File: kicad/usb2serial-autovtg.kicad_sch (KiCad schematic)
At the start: 38 parts, among them J2 Conn_01x04, J3 USB_C_Receptacle_USB2.0, U1 FT234XD, U3 74LVC1G17GW, U5 LMV358AIDGKR, U6 74LVC1G17GW

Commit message: 1.2V: wip
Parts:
- removed D4: BZX84C2V4LT1, Package_TO_SOT_SMD:SOT-23, symbol Diode:BZX84Cxx
- removed R15: 120, Resistor_SMD:R_0402_1005Metric, symbol Device:R
- removed U3, U6: 74LVC1G17GW, Package_SO:TSOP-5_1.65x3.05mm_P0.95mm, symbol ft234xd:74LVC1G17
- added U2, U4: 74LVC1T45GW, Package_TO_SOT_SMD:SOT-363_SC-70-6, symbol Logic_LevelTranslator:SN74LVC1T45DCK
- added U7: TLV74112PDBVR, Package_TO_SOT_SMD:SOT-23-5, symbol Regulator_Linear:TLV70012_SOT23-5
- C5: value 0.1u -> 1u
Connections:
- net +3V3: now also U2.1 (VCCA), U2.5 (DIR), U4.1 (VCCA), U7.1 (IN), U7.3 (EN)
- net GND: now also U2.2 (GND), U4.2 (GND), U4.5 (DIR), U7.2 (GND)
- net at U1.10 (RXD): now also U4.3 (A)
- net at U1.7 (TXD): now also U2.3 (A)
- net at R12.2, R3.1, R5.2: now also U4.4 (B)
- net at C10.1, R10.2: now also U2.6 (VCCB)
- net at R11.2: now also U2.4 (B)
- net +2V5 renamed +1V2
- net +1V2: now also U4.6 (VCCB), U7.5 (OUT)
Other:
- note added: "Vtarget range: 1.2V .. ~5.0V"
- note removed: "RX 74LVC1G17: @Vdd=2.5V: positive-going threshold: <=1.5V FT234 VddIO: 3.3V - positive-going threshold: <= 2.0V"
- note removed: "TX 74LVC1G17: @Vdd=5V: positive-going threshold: <=2.6V FT234 VddIO: 3.3V"
- note removed: "Vtarget range: 1.8V .. ~5.0V"
- moved on the sheet: C5, D1, R11, R12, R4, R5

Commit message: wip
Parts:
- added C7: 0.1u/10V, Capacitor_SMD:C_0402_1005Metric, symbol Device:C
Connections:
- net +3V3: now also C7.1
- net GND: now also C7.2
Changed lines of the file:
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@@
   (junction (at 189.23 137.16) (diameter 0) (color 0 0 0 0)
   )
+  (junction (at 163.83 123.19) (diameter 0) (color 0 0 0 0)
+  )
   (junction (at 86.36 153.67) (diameter 0) (color 0 0 0 0)
   )
@@
     (stroke (width 0) (type default))
   )
-  (wire (pts (xy 156.21 110.49) (xy 156.21 134.62))
+  (wire (pts (xy 139.7 110.49) (xy 139.7 134.62))
     (stroke (width 0) (type default))
   )
@@
     (stroke (width 0) (type default))
   )
+  (wire (pts (xy 163.83 123.19) (xy 163.83 127))
+    (stroke (width 0) (type default))
+  )
   (wire (pts (xy 102.87 33.02) (xy 118.11 33.02))
     (stroke (width 0) (type default))
@@
     (stroke (width 0) (type default))
   )
-  (wire (pts (xy 167.64 110.49) (xy 156.21 110.49))
+  (wire (pts (xy 167.64 110.49) (xy 139.7 110.49))
     (stroke (width 0) (type default))
   )
@@
     (stroke (width 0) (type default))
   )
-  (wire (pts (xy 156.21 134.62) (xy 135.89 134.62))
+  (wire (pts (xy 139.7 134.62) (xy 135.89 134.62))
     (stroke (width 0) (type default))
   )
@@
     )
   )
+  (symbol (lib_id "power:GND") (at 156.21 123.19 0) (unit 1)
+    (in_bom yes) (on_board yes) (dnp no)
+    (property "Reference" "#PWR036" (at 156.21 129.54 0)
+      (effects (font (size 1.27 1.27)) hide)
+    )
+    (property "Value" "GND" (at 156.337 127.5842 0)
+      (effects (font (size 1.27 1.27)))
+    )
+    (property "Footprint" "" (at 156.21 123.19 0)
+      (effects (font (size 1.27 1.27)) hide)
+    )
+    (property "Datasheet" "" (at 156.21 123.19 0)
+      (effects (font (size 1.27 1.27)) hide)
+    )
+    (pin "1")
+    (instances
+      (project "usb2serial-autovtg"
+        (path "/1f08e041-63eb-4c92-ae2b-bdba754c2965"
+          (reference "#PWR036") (unit 1)
+        )
+      )
+    )
+  )
   (symbol (lib_id "power:GND") (at 68.58 167.64 0) (unit 1)
     (in_bom yes) (on_board yes) (dnp no)
@@
     )
   )
-  (symbol (lib_id "power:+3V3") (at 163.83 127 0) (unit 1)
-    (in_bom yes) (on_board yes) (dnp no)
-    (property "Reference" "#PWR016" (at 163.83 130.81 0)
-      (effects (font (size 1.27 1.27)) hide)
-    )
-    (property "Value" "+3V3" (at 162.56 123.19 0)
-      (effects (font (size 1.27 1.27)))
-    )
-    (property "Footprint" "" (at 163.83 127 0)
-      (effects (font (size 1.27 1.27)) hide)
-    )
-    (property "Datasheet" "" (at 163.83 127 0)
+  (symbol (lib_id "power:+3V3") (at 163.83 123.19 0) (unit 1)
+    (in_bom yes) (on_board yes) (dnp no)
+    (property "Reference" "#PWR016" (at 163.83 127 0)
+      (effects (font (size 1.27 1.27)) hide)
+    )
+    (property "Value" "+3V3" (at 162.56 119.38 0)
+      (effects (font (size 1.27 1.27)))
+    )
+    (property "Footprint" "" (at 163.83 123.19 0)
+      (effects (font (size 1.27 1.27)) hide)
+    )
+    (property "Datasheet" "" (at 163.83 123.19 0)
       (effects (font (size 1.27 1.27)) hide)
     )
@@
         )
       )
+    )
+  )
+  (symbol (lib_id "Device:C") (at 160.02 123.19 270) (unit 1)
+    (in_bom yes) (on_board yes) (dnp no)
+    (property "Reference" "C7" (at 160.02 125.73 0)
+      (effects (font (size 1.27 1.27)) (justify left) hide)
+    )
+    (property "Value" "0.1u/10V" (at 149.86 119.38 90)
+      (effects (font (size 1.27 1.27)) (justify left))
+    )
+    (property "Footprint" "Capacitor_SMD:C_0402_1005Metric" (at 156.21 124.1552 0)
+      (effects (font (size 1.27 1.27)) hide)
+    )
+    (property "Datasheet" "" (at 160.02 123.19 0)
+      (effects (font (size 1.27 1.27)) hide)
+    )
+    (pin "1")
+    (pin "2")
+    (instances
+      (project "usb2serial-autovtg"
+        (path "/1f08e041-63eb-4c92-ae2b-bdba754c2965"
+          (reference "C7") (unit 1)
+        )
+      )

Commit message: add note regarding DIR pin
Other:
- note added: "DIR HIGH: A to B DIR LOW: B to A"
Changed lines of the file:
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@@
     (stroke (width 0) (type default))
+  )
+  (text "DIR HIGH: A to B\nDIR LOW: B to A" (at 189.23 100.33 0)
+    (effects (font (size 1.27 1.27) (thickness 0.254) bold) (justify left bottom))
   )
   (text "CBUS0 must be configured for ~{TX&RXLED} during production:\n  Option 1: http://www.ftdichip.com/Support/Utilities.htm#FT_Prog (Windows)\n  Option 2: https://github.com/richardeoin/ftx-prog (Linux)"

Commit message: finalize rev3
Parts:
- C5: value 1u -> 4.7u/10V
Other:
- note removed: "BZX84C2V4LT1: I_{ZT}: ~6.5mA => V_{Z}: ~2.5V"
- moved on the sheet: C5, U7
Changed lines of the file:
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@@
   (title_block
     (title "USB2serial AutoVtg")
-    (date "2023-07-28")
-    (rev "v2")
+    (date "2024-01-23")
+    (rev "v3")
     (comment 1 "     https://creativecommons.org/licenses/by-sa/4.0/deed.en")
     (comment 2 "License: Creative Commons Attribution/Share-Alike 4.0")
     (comment 3 "Designed by: Benedikt Heinz <hunz at mailbox.org>")
   )
-  (junction (at 26.67 26.67) (diameter 0) (color 0 0 0 0)
+  (junction (at 43.18 34.29) (diameter 0) (color 0 0 0 0)
   )
   (junction (at 231.14 130.81) (diameter 0) (color 0 0 0 0)
@@
   (junction (at 88.9 85.09) (diameter 0) (color 0 0 0 0)
   )
-  (junction (at 44.45 26.67) (diameter 0) (color 0 0 0 0)
+  (junction (at 60.96 34.29) (diameter 0) (color 0 0 0 0)
   )
   (junction (at 166.37 147.32) (diameter 0) (color 0 0 0 0)
@@
     (stroke (width 0) (type default))
   )
-  (wire (pts (xy 26.67 24.13) (xy 26.67 26.67))
-    (stroke (width 0) (type default))
-  )
-  (wire (pts (xy 26.67 26.67) (xy 26.67 29.21))
+  (wire (pts (xy 43.18 31.75) (xy 43.18 34.29))
+    (stroke (width 0) (type default))
+  )
+  (wire (pts (xy 43.18 34.29) (xy 43.18 36.83))
     (stroke (width 0) (type default))
   )
@@
     (stroke (width 0) (type default))
   )
-  (wire (pts (xy 41.91 26.67) (xy 44.45 26.67))
+  (wire (pts (xy 58.42 34.29) (xy 60.96 34.29))
     (stroke (width 0) (type default))
   )
@@
     (at 100.33 167.64 0)
     (effects (font (size 1.27 1.27)) (justify left bottom) (href "https://github.com/richardeoin/ftx-prog"))
-  )
-  (text "BZX84C2V4LT1:\n  I_{ZT}: ~6.5mA => V_{Z}: ~2.5V" (at 53.34 58.42 0)
-    (effects (font (size 1.27 1.27)) (justify left bottom))
   )
   (text "SBOS923H (TI LMV3xxA / 6.1 Absolute Maximum Ratings) states:\n Input pins are diode-clamped to the power-supply rails.\n Input signals that may swing more than 0.5 V beyond the\n supply rails must be current limited to 10 mA or less.\n\nR6 limits the clamping current when VTG is supplied\n with no USB supply connected."
@@
     )
   )
-  (symbol (lib_id "power:GND") (at 34.29 36.83 0) (unit 1)
-    (in_bom yes) (on_board yes) (dnp no)
-    (property "Reference" "#PWR034" (at 34.29 43.18 0)
-      (effects (font (size 1.27 1.27)) hide)
-    )
-    (property "Value" "GND" (at 34.417 41.2242 0)
-      (effects (font (size 1.27 1.27)))
-    )
-    (property "Footprint" "" (at 34.29 36.83 0)
-      (effects (font (size 1.27 1.27)) hide)
-    )
-    (property "Datasheet" "" (at 34.29 36.83 0)
+  (symbol (lib_id "power:GND") (at 50.8 44.45 0) (unit 1)
+    (in_bom yes) (on_board yes) (dnp no)
+    (property "Reference" "#PWR034" (at 50.8 50.8 0)
+      (effects (font (size 1.27 1.27)) hide)
+    )
+    (property "Value" "GND" (at 50.927 48.8442 0)
+      (effects (font (size 1.27 1.27)))
+    )
+    (property "Footprint" "" (at 50.8 44.45 0)
+      (effects (font (size 1.27 1.27)) hide)
+    )
+    (property "Datasheet" "" (at 50.8 44.45 0)
       (effects (font (size 1.27 1.27)) hide)
     )
@@
     )
   )
-  (symbol (lib_id "power:GND") (at 44.45 34.29 0) (unit 1)
-    (in_bom yes) (on_board yes) (dnp no)
-    (property "Reference" "#PWR015" (at 44.45 40.64 0)
-      (effects (font (size 1.27 1.27)) hide)
-    )
-    (property "Value" "GND" (at 44.577 38.6842 0)
-      (effects (font (size 1.27 1.27)))
-    )
-    (property "Footprint" "" (at 44.45 34.29 0)
-      (effects (font (size 1.27 1.27)) hide)
-    )
-    (property "Datasheet" "" (at 44.45 34.29 0)
+  (symbol (lib_id "power:GND") (at 60.96 41.91 0) (unit 1)
+    (in_bom yes) (on_board yes) (dnp no)
+    (property "Reference" "#PWR015" (at 60.96 48.26 0)
+      (effects (font (size 1.27 1.27)) hide)
+    )
+    (property "Value" "GND" (at 61.087 46.3042 0)
+      (effects (font (size 1.27 1.27)))
+    )
+    (property "Footprint" "" (at 60.96 41.91 0)
+      (effects (font (size 1.27 1.27)) hide)
+    )
+    (property "Datasheet" "" (at 60.96 41.91 0)
       (effects (font (size 1.27 1.27)) hide)
     )
@@
     )
   )
-  (symbol (lib_id "Device:C") (at 44.45 30.48 0) (unit 1)
-    (in_bom yes) (on_board yes) (dnp no)
-    (property "Reference" "C5" (at 47.3456 29.3116 0)
-      (effects (font (size 1.27 1.27)) (justify left))
-    )
-    (property "Value" "1u" (at 47.3456 31.623 0)
-      (effects (font (size 1.27 1.27)) (justify left))
-    )
-    (property "Footprint" "Capacitor_SMD:C_0402_1005Metric" (at 45.4152 34.29 0)
-      (effects (font (size 1.27 1.27)) hide)
-    )
-    (property "Datasheet" "" (at 44.45 30.48 0)
+  (symbol (lib_id "Device:C") (at 60.96 38.1 0) (unit 1)
+    (in_bom yes) (on_board yes) (dnp no)
+    (property "Reference" "C5" (at 63.8556 36.9316 0)
+      (effects (font (size 1.27 1.27)) (justify left))
+    )
+    (property "Value" "4.7u/10V" (at 63.8556 39.243 0)
+      (effects (font (size 1.27 1.27)) (justify left))
+    )
+    (property "Footprint" "Capacitor_SMD:C_0402_1005Metric" (at 61.9252 41.91 0)
+      (effects (font (size 1.27 1.27)) hide)
+    )
+    (property "Datasheet" "" (at 60.96 38.1 0)
       (effects (font (size 1.27 1.27)) hide)
     )
@@
     )
   )
-  (symbol (lib_id "power:+3V3") (at 26.67 24.13 0) (unit 1)
-    (in_bom yes) (on_board yes) (dnp no)
-    (property "Reference" "#PWR017" (at 26.67 27.94 0)
-      (effects (font (size 1.27 1.27)) hide)
-    )
-    (property "Value" "+3V3" (at 26.67 20.32 0)
-      (effects (font (size 1.27 1.27)))
-    )
-    (property "Footprint" "" (at 26.67 24.13 0)
-      (effects (font (size 1.27 1.27)) hide)
-    )
-    (property "Datasheet" "" (at 26.67 24.13 0)
+  (symbol (lib_id "power:+3V3") (at 43.18 31.75 0) (unit 1)
+    (in_bom yes) (on_board yes) (dnp no)
+    (property "Reference" "#PWR017" (at 43.18 35.56 0)
+      (effects (font (size 1.27 1.27)) hide)
+    )
+    (property "Value" "+3V3" (at 43.18 27.94 0)
+      (effects (font (size 1.27 1.27)))
+    )
+    (property "Footprint" "" (at 43.18 31.75 0)
+      (effects (font (size 1.27 1.27)) hide)
+    )
+    (property "Datasheet" "" (at 43.18 31.75 0)
       (effects (font (size 1.27 1.27)) hide)
     )
@@
     )
   )
-  (symbol (lib_id "power:+1V2") (at 44.45 26.67 0) (unit 1)
+  (symbol (lib_id "power:+1V2") (at 60.96 34.29 0) (unit 1)
     (in_bom yes) (on_board yes) (dnp no) (fields_autoplaced)
-    (property "Reference" "#PWR03" (at 44.45 30.48 0)
-      (effects (font (size 1.27 1.27)) hide)
-    )
-    (property "Value" "+1V2" (at 44.45 21.59 0)
-      (effects (font (size 1.27 1.27)))
-    )
-    (property "Footprint" "" (at 44.45 26.67 0)
-      (effects (font (size 1.27 1.27)) hide)
-    )
-    (property "Datasheet" "" (at 44.45 26.67 0)
+    (property "Reference" "#PWR03" (at 60.96 38.1 0)
+      (effects (font (size 1.27 1.27)) hide)
+    )
+    (property "Value" "+1V2" (at 60.96 29.21 0)
+      (effects (font (size 1.27 1.27)))
+    )
+    (property "Footprint" "" (at 60.96 34.29 0)
+      (effects (font (size 1.27 1.27)) hide)
+    )
+    (property "Datasheet" "" (at 60.96 34.29 0)
       (effects (font (size 1.27 1.27)) hide)
     )
@@
     )
   )
-  (symbol (lib_id "Regulator_Linear:TLV70012_SOT23-5") (at 34.29 29.21 0) (unit 1)
-    (in_bom yes) (on_board yes) (dnp no)
-    (property "Reference" "U7" (at 26.67 34.29 0)
-      (effects (font (size 1.27 1.27)))
-    )
-    (property "Value" "TLV74112PDBVR" (at 24.13 36.83 0)
-      (effects (font (size 1.27 1.27)))
-    )
-    (property "Footprint" "Package_TO_SOT_SMD:SOT-23-5" (at 34.29 20.955 0)
+  (symbol (lib_id "Regulator_Linear:TLV70012_SOT23-5") (at 50.8 36.83 0) (unit 1)
+    (in_bom yes) (on_board yes) (dnp no)
+    (property "Reference" "U7" (at 43.18 41.91 0)
+      (effects (font (size 1.27 1.27)))
+    )
+    (property "Value" "TLV74112PDBVR" (at 40.64 44.45 0)
+      (effects (font (size 1.27 1.27)))
+    )
+    (property "Footprint" "Package_TO_SOT_SMD:SOT-23-5" (at 50.8 28.575 0)
       (effects (font (size 1.27 1.27) italic) hide)
     )
-    (property "Datasheet" "http://www.ti.com/lit/ds/symlink/tlv700.pdf" (at 34.29 27.94 0)
-      (effects (font (size 1.27 1.27)) hide)
-    )
+    (property "Datasheet" "http://www.ti.com/lit/ds/symlink/tlv700.pdf" (at 50.8 35.56 0)
+      (effects (font (size 1.27 1.27)) hide)
+    )

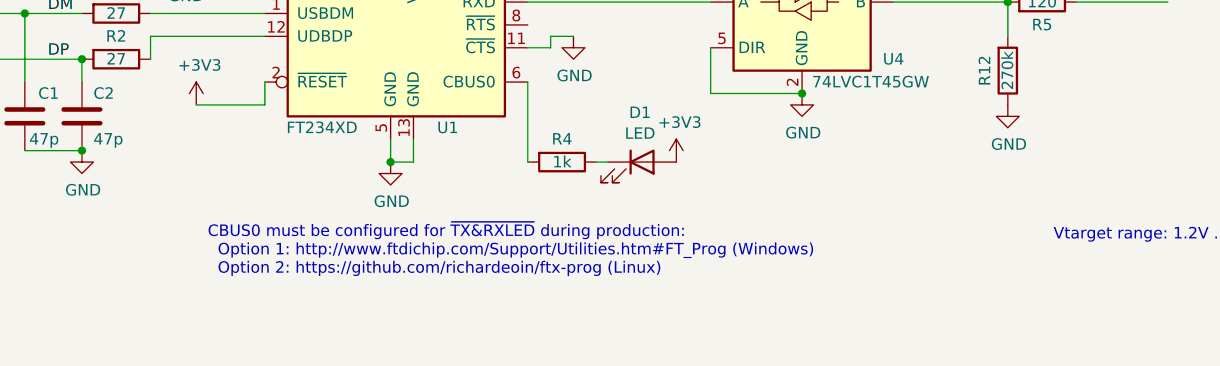
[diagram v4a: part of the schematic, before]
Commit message: add ftx-prog command
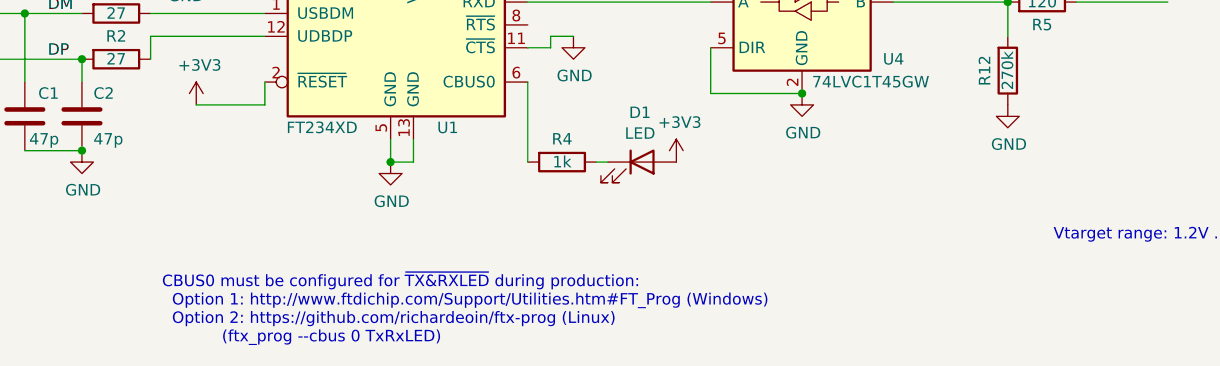
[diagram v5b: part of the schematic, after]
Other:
- note added: "CBUS0 must be configured for ~{TX&RXLED} during production: Option 1: http://www.ftdichip.com/Support/Utilities.htm#FT_Prog (Windows) Option 2: https://github.com/richardeoin/ftx-prog (Linux) (ftx_prog --cbus 0 TxRxLED)"
- note removed: "CBUS0 must be configured for ~{TX&RXLED} during production: Option 1: http://www.ftdichip.com/Support/Utilities.htm#FT_Prog (Windows) Option 2: https://github.com/richardeoin/ftx-prog (Linux)"
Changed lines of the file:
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@@
     (effects (font (size 1.27 1.27) (thickness 0.254) bold) (justify left bottom))
   )
-  (text "CBUS0 must be configured for ~{TX&RXLED} during production:\n  Option 1: http://www.ftdichip.com/Support/Utilities.htm#FT_Prog (Windows)\n  Option 2: https://github.com/richardeoin/ftx-prog (Linux)"
-    (at 100.33 167.64 0)
+  (text "CBUS0 must be configured for ~{TX&RXLED} during production:\n  Option 1: http://www.ftdichip.com/Support/Utilities.htm#FT_Prog (Windows)\n  Option 2: https://github.com/richardeoin/ftx-prog (Linux)\n            (ftx_prog --cbus 0 TxRxLED)"
+    (at 95.25 175.26 0)
     (effects (font (size 1.27 1.27)) (justify left bottom) (href "https://github.com/richardeoin/ftx-prog"))
   )
